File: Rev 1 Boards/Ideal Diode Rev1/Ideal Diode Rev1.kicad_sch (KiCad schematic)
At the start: 0 parts

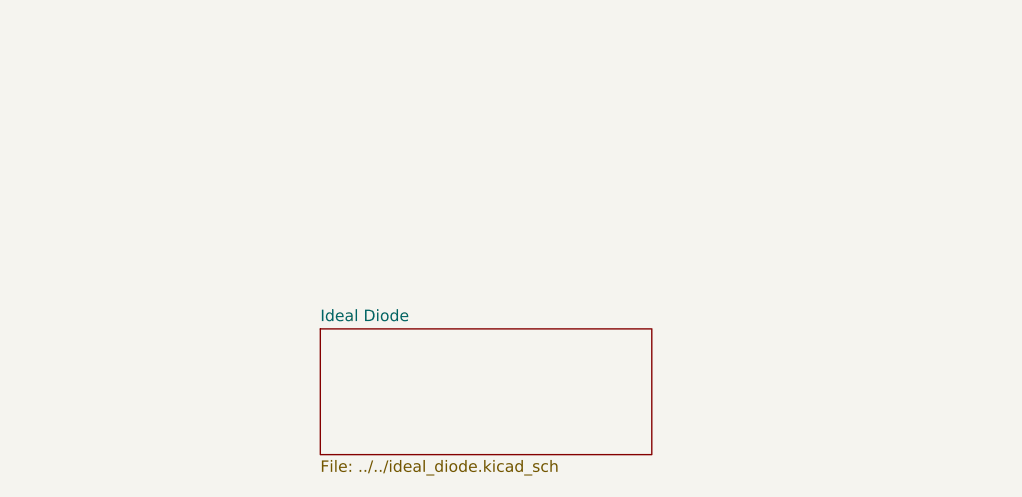
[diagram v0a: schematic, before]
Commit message: began ideal diode layout
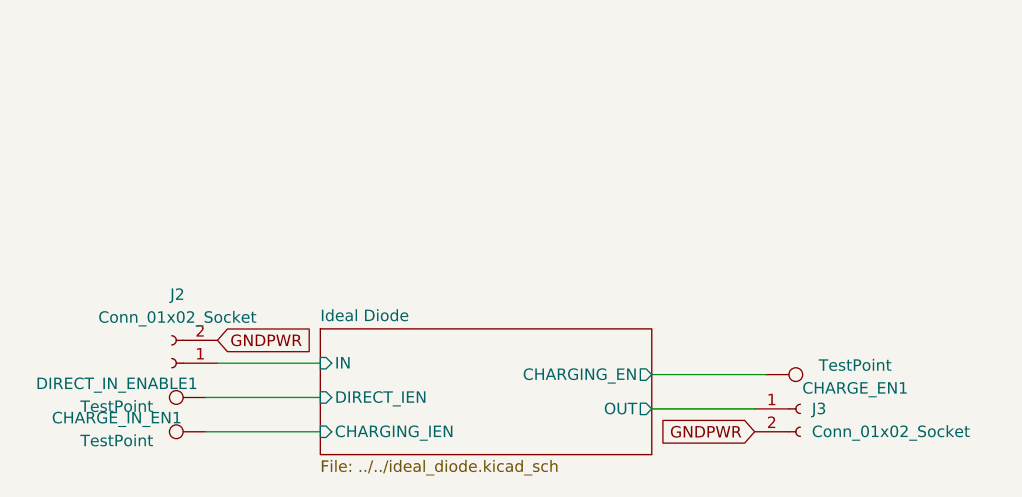
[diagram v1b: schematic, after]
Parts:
- added CHARGE_EN1, CHARGE_IN_EN1, DIRECT_IN_ENABLE1: TestPoint, TestPoint:TestPoint_Keystone_5010-5014_Multipurpose, symbol Connector:TestPoint
- added J2, J3: Conn_01x02_Socket, Connector:Banana_Jack_2Pin, symbol Connector:Conn_01x02_Socket
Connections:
- new net GNDPWR: J2.2 (Pin_2), J3.2 (Pin_2)
- new net Ideal Diode/CHARGING_EN: CHARGE_EN1.1
- new net Ideal Diode/CHARGING_IEN: CHARGE_IN_EN1.1
- new net Ideal Diode/DIRECT_IEN: DIRECT_IN_ENABLE1.1
- new net Ideal Diode/IN: J2.1 (Pin_1)
- new net Ideal Diode/OUT: J3.1 (Pin_1)
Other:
- sheet Ideal Diode ports: added CHARGING_EN, CHARGING_IEN, DIRECT_IEN, IN, OUT; removed none

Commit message: finished ideal diode layout
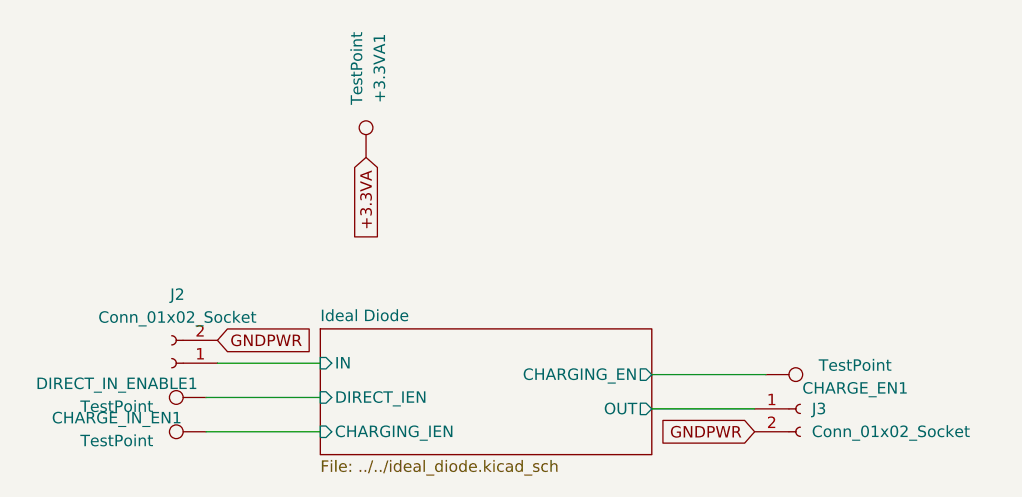
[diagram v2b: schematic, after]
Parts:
- added +3.3VA1: TestPoint, TestPoint:TestPoint_Keystone_5010-5014_Multipurpose, symbol Connector:TestPoint
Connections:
- new net +3.3VA: +3.3VA1.1
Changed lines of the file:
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@@
+		)
+	)
+	(global_label "+3.3VA"
+		(shape input)
+		(at 82.55 78.74 270)
+		(fields_autoplaced yes)
+		(effects
+			(font
+				(size 1.27 1.27)
+			)
+			(justify right)
+		)
+		(property "Intersheetrefs" "${INTERSHEET_REFS}"
+			(at 82.55 88.4986 90)
+			(effects
+				(font
+					(size 1.27 1.27)
+				)
+				(justify right)
+				(hide yes)
+			)
 		)
 	)
@@
 					(unit 1)
 				)
+			)
+		)
+	)
+	(symbol
+		(lib_id "Connector:TestPoint")
+		(at 82.55 78.74 0)
+		(unit 1)
+		(exclude_from_sim no)
+		(in_bom yes)
+		(on_board yes)
+		(dnp no)
+		(property "Reference" "+3.3VA1"
+			(at 84.074 68.834 90)
+			(effects
+				(font
+					(size 1.27 1.27)
+				)
+			)
+		)
+		(property "Value" "TestPoint"
+			(at 81.534 68.834 90)
+			(effects
+				(font
+					(size 1.27 1.27)
+				)
+			)
+		)
+		(property "Footprint" "TestPoint:TestPoint_Keystone_5010-5014_Multipurpose"
+			(at 87.63 78.74 0)
+			(effects
+				(font
+					(size 1.27 1.27)
+				)
+				(hide yes)
+			)
+		)
+		(property "Datasheet" "~"
+			(at 87.63 78.74 0)
+			(effects
+				(font
+					(size 1.27 1.27)
+				)
+				(hide yes)
+			)
+		)
+		(property "Description" "test point"
+			(at 82.55 78.74 0)
+			(effects
+				(font
+					(size 1.27 1.27)
+				)
+				(hide yes)
+			)
+		)
+		(pin "1"
+		)
+		(instances
+			(project "Ideal Diode Rev1"
+				(path "/1958bbb1-b715-4a10-a229-bee0eabb28b0"
+					(reference "+3.3VA1")
+					(unit 1)
+				)
